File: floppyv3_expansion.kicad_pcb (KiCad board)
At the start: 2 copper layers, 1 part

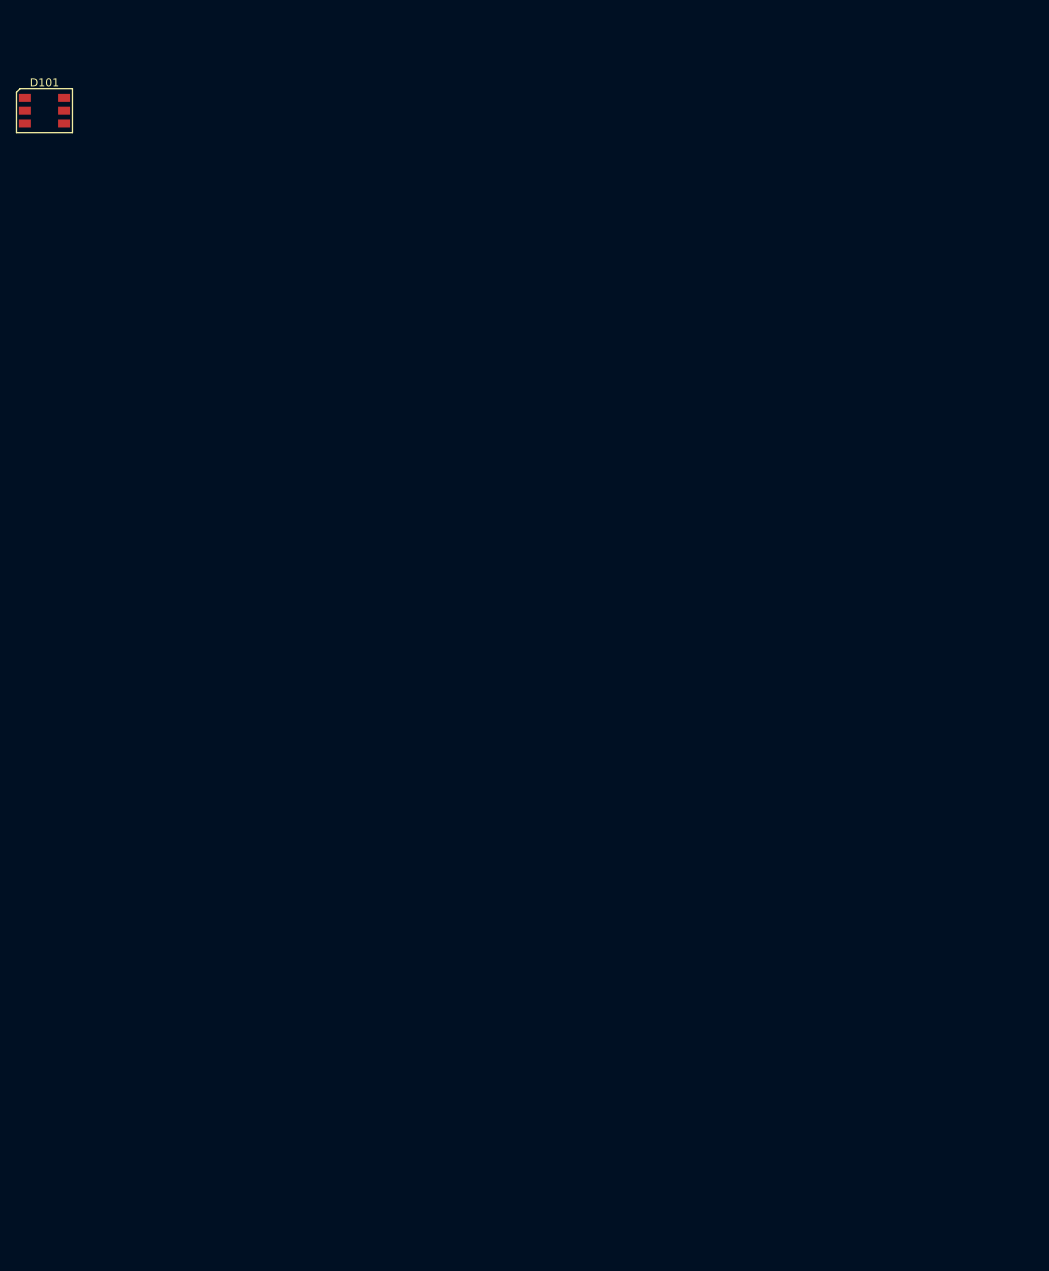
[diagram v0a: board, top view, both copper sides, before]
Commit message: Started layout
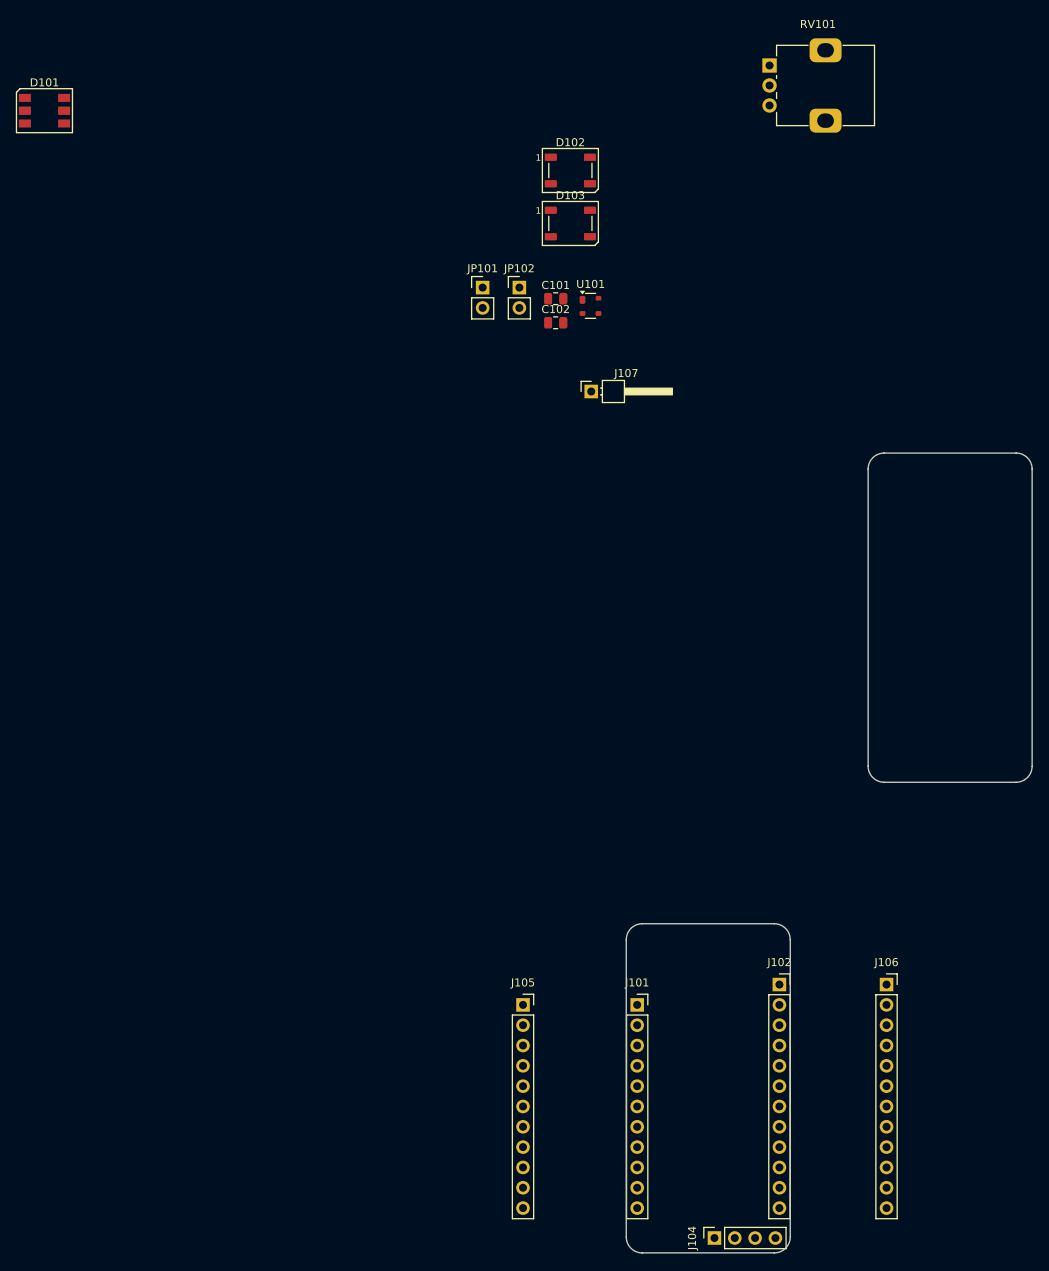
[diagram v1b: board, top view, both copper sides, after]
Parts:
- added C101: 0.1u, Capacitor_SMD:C_0805_2012Metric, F.Cu at (116.9, 71.1)
- added C102: 0.1u, Capacitor_SMD:C_0805_2012Metric, F.Cu at (116.9, 74.1)
- added D102: USR_LED1, LED_SMD:LED_WS2812B_PLCC4_5.0x5.0mm_P3.2mm, F.Cu at (118.7, 55.1)
- added D103: USR_LED2, LED_SMD:LED_WS2812B_PLCC4_5.0x5.0mm_P3.2mm, F.Cu at (118.7, 61.7)
- added J101: Left_Bank_Board_Socket, Connector_PinSocket_2.54mm:PinSocket_1x11_P2.54mm_Vertical, F.Cu at (127.1, 159.4)
- added J102: Right_Bank_Board_Socket, Connector_PinSocket_2.54mm:PinSocket_1x12_P2.54mm_Vertical, F.Cu at (144.8, 156.9)
- added J104: STLink_Board_Conn, Connector_PinSocket_2.54mm:PinSocket_1x04_P2.54mm_Vertical, F.Cu at (136.7, 188.5)
- added J105: Left_Bank_Free_Socket, Connector_PinSocket_2.54mm:PinSocket_1x11_P2.54mm_Vertical, F.Cu at (112.8, 159.4)
- added J106: Right_Bank_Free_Socket, Connector_PinSocket_2.54mm:PinSocket_1x12_P2.54mm_Vertical, F.Cu at (158.2, 156.9)
- added J107: POT_OUT, Connector_PinHeader_2.54mm:PinHeader_1x01_P2.54mm_Horizontal, F.Cu at (121.3, 82.7)
- added JP101: BTN_JMP, Connector_PinHeader_2.54mm:PinHeader_1x02_P2.54mm_Vertical, F.Cu at (107.7, 69.7)
- added JP102: LED_JMP, Connector_PinHeader_2.54mm:PinHeader_1x02_P2.54mm_Vertical, F.Cu at (112.3, 69.7)
- added RV101: USR_POT, Potentiometer_THT:Potentiometer_Alps_RK09K_Single_Vertical, F.Cu at (143.6, 42.0)
- added U101: MAX6816, Package_TO_SOT_SMD:SOT-143, F.Cu at (121.2, 72.0)
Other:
- board outline added: 50.7 x 100 mm

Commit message: Starting to layout components
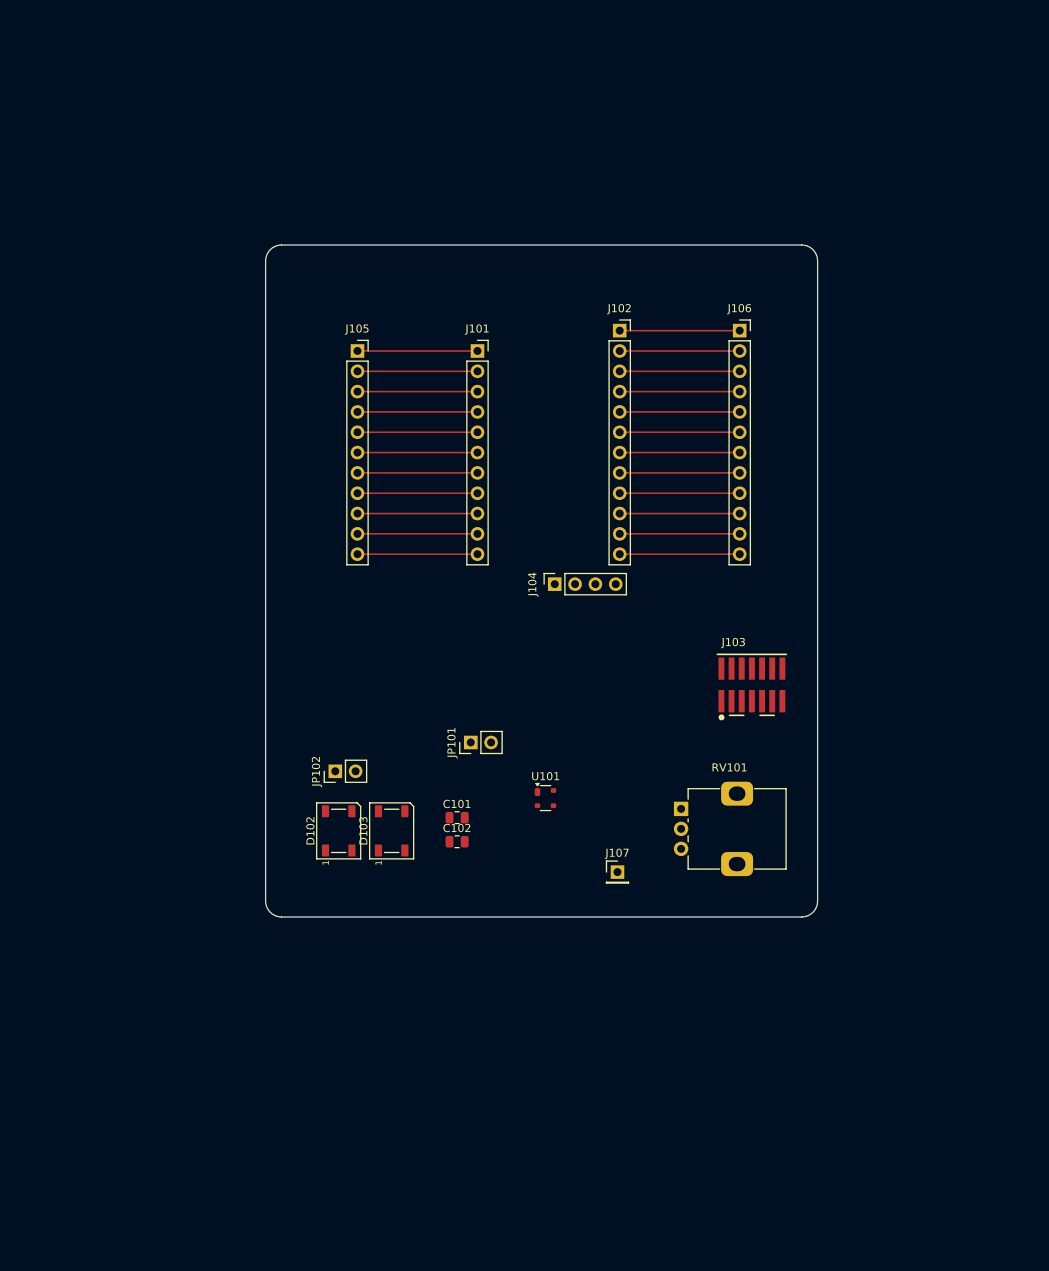
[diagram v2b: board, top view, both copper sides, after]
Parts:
- removed D101: WS2812, LED_SMD:LED_WS2812_PLCC6_5.0x5.0mm_P1.6mm
- added J103: FTSH-107-01-L-DV-K-TR, SAMTEC_FTSH-107-01-L-DV-K-TR:SAMTEC_FTSH-107-01-L-DV-K-TR, F.Cu at (141.4, 119.4)
- J107: footprint Connector_PinHeader_2.54mm:PinHeader_1x01_P2.54mm_Horizontal -> Connector_PinHeader_2.54mm:PinHeader_1x01_P2.54mm_Vertical
- moved RV101 93.6 mm to (132.6, 134.9)
- moved D102 87.5 mm to (89.8, 137.7), turned to 90 degrees
- moved J105 84.3 mm to (92.1, 77.7)
- moved J101 84.1 mm to (107.1, 77.7)
- moved J102 84.1 mm to (124.9, 75.1)
- moved J104 84.1 mm to (116.8, 106.8)
- moved J106 83.8 mm to (139.9, 75.1)
- moved D103 79.1 mm to (96.4, 137.7), turned to 90 degrees
- moved C101 66.0 mm to (104.5, 136.0)
- moved C102 66.0 mm to (104.5, 139.0)
- moved JP102 64.7 mm to (89.3, 130.2), turned to 90 degrees
- moved U101 61.8 mm to (115.6, 133.6)
- moved J107 60.2 mm to (124.6, 142.8)
- moved JP101 56.9 mm to (106.3, 126.6), turned to 90 degrees
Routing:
- net GND: track 0.00 -> 29.3 mm
- net /VUSB: track 0.00 -> 15.0 mm
- net /VIN: track 0.00 -> 15.0 mm
- net /PB3: track 0.00 -> 15.0 mm
- net /PB0: track 0.00 -> 15.0 mm
- net /PA7: track 0.00 -> 15.0 mm
- net /PA6: track 0.00 -> 15.0 mm
- net /PA5: track 0.00 -> 15.0 mm
- net /PA14: track 0.00 -> 15.0 mm
- net /PA13: track 0.00 -> 15.0 mm
- net /PA12: track 0.00 -> 15.0 mm
- net /PA11: track 0.00 -> 15.0 mm
- net /PC15: track 0.00 -> 14.3 mm
- net /PC14: track 0.00 -> 14.3 mm
- net /PB7: track 0.00 -> 14.3 mm
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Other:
- board size 50.7 x 100 mm -> 69 x 84 mm

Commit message: Further improvements to layout and schematic
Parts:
- removed J107: POT_OUT, Connector_PinHeader_2.54mm:PinHeader_1x01_P2.54mm_Vertical
- added H1: MountingHole, MountingHole:MountingHole_2.2mm_M2_Pad_Via, F.Cu at (85.1, 68.9)
- added H2: MountingHole, MountingHole:MountingHole_2.2mm_M2_Pad_Via, F.Cu at (145.1, 68.9)
- added H3: MountingHole, MountingHole:MountingHole_2.2mm_M2_Pad_Via, F.Cu at (145.1, 128.9)
- added H4: MountingHole, MountingHole:MountingHole_2.2mm_M2_Pad_Via, F.Cu at (85.1, 128.9)
- added JP1: POT_JMP, Connector_PinHeader_2.54mm:PinHeader_1x02_P2.54mm_Vertical, F.Cu at (134.5, 128.8)
- added SW1: USR_BTN, Button_Switch_THT:SW_PUSH-12mm, F.Cu at (108.9, 116.3)
- C1: renamed from C101; moved to B.Cu
- C2: renamed from C102; moved to B.Cu
- J6: renamed from J103; moved to B.Cu
- U1: renamed from U101; moved to B.Cu
- moved J6 40.1 mm to (115.1, 89.2), turned to 180 degrees
- moved C2 24.0 mm to (93.0, 118.0), turned to -90 degrees
- moved RV1 23.2 mm to (138.1, 112.3), turned to -90 degrees
- moved D1 20.9 mm to (96.9, 118.0)
- moved D2 20.9 mm to (89.0, 118.1)
- moved C1 18.9 mm to (115.1, 120.4)
- moved U1 15.9 mm to (115.2, 117.7), turned to -90 degrees
- moved JP2 6.95 mm to (104.8, 119.8), turned to 180 degrees
- moved JP3 6.93 mm to (95.5, 127.0), turned to -90 degrees
- moved J5 0.88 mm to (139.0, 75.0)
- moved J3 0.88 mm to (115.9, 106.7)
- moved J1 0.88 mm to (91.2, 77.6)
- moved J2 0.88 mm to (106.2, 77.6)
- moved J4 0.88 mm to (124.0, 75.0)
- renumbered D102 to D1, D103 to D2, J105 to J1, J101 to J2, J104 to J3, J102 to J4, J106 to J5, JP101 to JP2, JP102 to JP3, RV101 to RV1
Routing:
- net GND: track 29.3 -> 0.00 mm
- net /VUSB: track 15.0 -> 0.00 mm
- net /VIN: track 15.0 -> 0.00 mm
- net /PB3: track 15.0 -> 0.00 mm
- net /PB0: track 15.0 -> 0.00 mm
- net /PA7: track 15.0 -> 0.00 mm
- net /PA6: track 15.0 -> 0.00 mm
- net /PA5: track 15.0 -> 0.00 mm
- net /PA14: track 15.0 -> 0.00 mm
- net /PA13: track 15.0 -> 0.00 mm
- net /PA12: track 15.0 -> 0.00 mm
- net /PA11: track 15.0 -> 0.00 mm
- net /PC15: track 14.3 -> 0.00 mm
- net /PC14: track 14.3 -> 0.00 mm
- net /PB7: track 14.3 -> 0.00 mm
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- added copper zone on B.Cu, net GND
- added copper zone on F.Cu, net GND
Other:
- board size 69 x 84 mm -> 69 x 69 mm

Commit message: Added final (?) touches to layout
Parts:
- moved JP1 19.1 mm to (137.9, 110.0)
- moved JP3 16.8 mm to (97.8, 110.4)
- moved C1 2.76 mm to (115.2, 117.6)
- moved U1 2.66 mm to (115.1, 120.3), turned to 180 degrees
- moved D2 1.82 mm to (87.2, 118.1)
- moved RV1 1.20 mm to (138.1, 113.5)
- moved C2 1.16 mm to (91.8, 118.0), turned to 90 degrees
- turned J6 to 0 degrees
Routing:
- net /3V3: track 0.00 -> 135.3 mm, vias 0 -> 2
- net /PB0: track 0.00 -> 47.5 mm
- net /PA0: track 0.00 -> 41.4 mm, vias 0 -> 1
- net /NRST: track 0.00 -> 30.6 mm, vias 0 -> 1
- net /T_SWD: track 0.00 -> 22.9 mm, vias 0 -> 2
- net /PA5: track 0.00 -> 22.6 mm
- net Net-(U1-IN): track 0.00 -> 18.3 mm
- net /T_SCK: track 0.00 -> 17.4 mm
- net /PC15: track 0.00 -> 15.0 mm
- net /PC14: track 0.00 -> 15.0 mm
- net /PB7: track 0.00 -> 15.0 mm
- net /PA4: track 0.00 -> 15.0 mm
- net /PA3: track 0.00 -> 15.0 mm
- net /PA2: track 0.00 -> 15.0 mm
- net /PA1: track 0.00 -> 15.0 mm
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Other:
- board text added: "BUTTON"
- board text added: "LEDs"
- board text added: "POTENTIOMETER"
- board text added: "USART2"
